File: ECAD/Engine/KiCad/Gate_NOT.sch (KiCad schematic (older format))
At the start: 2 parts, among them Q427 BSS84, Q428 2N7002

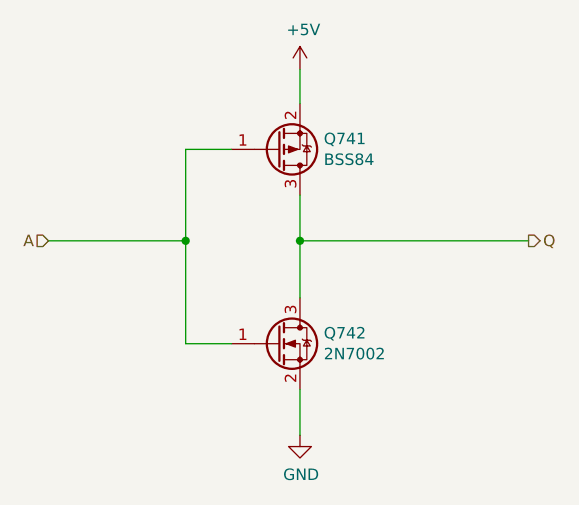
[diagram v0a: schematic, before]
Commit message: Engine: Added Tooling Holes, LCSC Part numbers
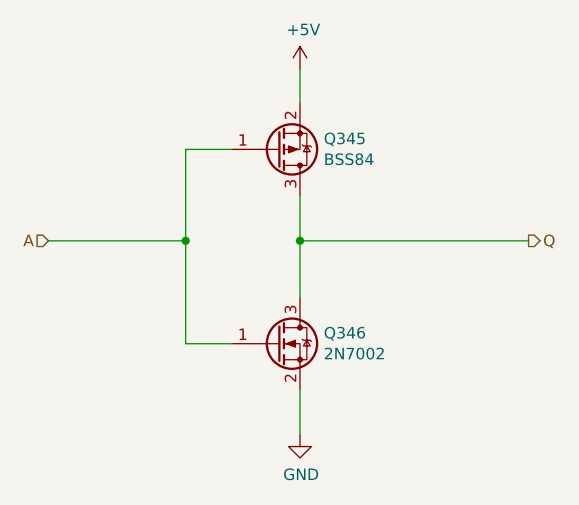
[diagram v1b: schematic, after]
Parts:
- Q427: LCSC (none) -> C114481
- Q428: LCSC (none) -> C8545
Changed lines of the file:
@@
 AR Path="/6073F2D8/606FFABF/60756041/6075603F/5E55601B" Ref="Q381"  Part="1"
 AR Path="/6073F2D8/606FFAC7/60756041/6075603F/5E55601B" Ref="Q395"  Part="1"
-F 0 "Q741" H 4254 3304 50  0000 L CNN
+F 0 "Q345" H 4254 3304 50  0000 L CNN
 F 1 "BSS84" H 4254 3395 50  0000 L CNN
 F 2 "LogicQ:SOT-23-P" H 4250 3450 50  0001 C CNN
 F 3 "~" H 4050 3350 50  0001 C CNN
+F 4 "C114481" H 4050 3350 50  0001 C CNN "LCSC"
 	1    4050 3350
 	1    0    0    1
@@
 AR Path="/6073F2D8/606FFABF/60756041/6075603F/60D7A8D4" Ref="Q382"  Part="1"
 AR Path="/6073F2D8/606FFAC7/60756041/6075603F/60D7A8D4" Ref="Q396"  Part="1"
-F 0 "Q742" H 4254 4246 50  0000 L CNN
+F 0 "Q346" H 4254 4246 50  0000 L CNN
 F 1 "2N7002" H 4254 4155 50  0000 L CNN
 F 2 "LogicQ:SOT-23-N" H 4250 4300 50  0001 C CNN
 F 3 "~" H 4050 4200 50  0001 C CNN
+F 4 "C8545" H 4050 4200 50  0001 C CNN "LCSC"
 	1    4050 4200
 	1    0    0    -1
